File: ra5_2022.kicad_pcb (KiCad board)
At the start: 2 copper layers, 123 parts, among them CN1 KF250-3.5-2P-2, J1 USB_C_Receptacle, J2 MX15EDGRHC-3.5-2x03P, Q1 PJM2309PSC, SW1 SW_Push, SW2 SW_Push, U1 AP63203WU, U10 DB126V-5.0-2P-BK-P, U2 B0303S-1W_C883455, U3 ESP32-C6-MINI-1, U4 AMS1117-3.3, U5 ATM90E32AS-AU-R, U6 K3-2268P, U7 TLP291-4, U8 TLP291-4, U9 DB126V-5.0-2P-BK-P, Y1 ABM8G-16.384MHZ-18-D2Y-T

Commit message: Add MX15EDGRHC-3.5-2x03P footprint and update M90E32AS connector
Adds the new project-local footprint and repoints the M90E32AS
6-pin connector to it, plus resulting PCB layout and project
metadata updates.

Co-Authored-By: Claude Sonnet 5 <noreply@anthropic.com>
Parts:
- J2: footprint ra5_2022:CONN-TH_6P-P3.50x2.50_MAX_MX15EDGRHC-3.5-2x03P -> ra5_2022:MX15EDGRHC-3.5-2x03P
- moved J2 2.61 mm to (183.2, 100.0)
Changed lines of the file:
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@@
 		)
 	)
-	(footprint "ra5_2022:CONN-TH_6P-P3.50x2.50_MAX_MX15EDGRHC-3.5-2x03P"
+	(footprint "ra5_2022:MX15EDGRHC-3.5-2x03P"
 		(layer "F.Cu")
-		(at 184.775 102.075 90)
-		(descr "MAX (Cixi Maixu) MX15EDGRHC-3.5-2*03P-BK01-Cu-A, 6 position board-side header socket, right angle, THT, 3.5mm pitch (columns), 2.5mm row pitch, drill 1.4mm. Pad layout hand-derived from single-page mechanical datasheet (no explicit pinout diagram) - VERIFY against physical part/pin1 marking before fabrication. LCSC C49142489")
-		(tags "THT Terminal Block MAX MX15EDGRHC-3.5 2x03P pitch 3.5mm row 2.5mm drill 1.4mm C49142489")
+		(at 183.2 100 90)
 		(property "Reference" "J2"
-			(at 0 -4.8 90)
+			(at 0 -8.3 90)
+			(unlocked yes)
 			(layer "F.SilkS")
 			(effects
 				(font
 					(size 1 1)
-					(thickness 0.15)
+					(thickness 0.1)
 				)
 			)
 		)
 		(property "Value" "MX15EDGRHC-3.5-2x03P"
-			(at 0 4.8 90)
+			(at 0 -10.3 90)
+			(unlocked yes)
 			(layer "F.Fab")
 			(effects
@@
 		(property "Datasheet" "https://datasheet.lcsc.com/datasheet/pdf/3e53538744bd12542cc29a45b22c9fbc.pdf?productCode=C49142489"
 			(at 0 0 90)
+			(unlocked yes)
 			(layer "F.Fab")
 			(hide yes)
 			(effects
 				(font
-					(size 1.27 1.27)
+					(size 1 1)
+					(thickness 0.15)
 				)
 			)
@@
 		(property "Description" ""
 			(at 0 0 90)
+			(unlocked yes)
 			(layer "F.Fab")
 			(hide yes)
 			(effects
 				(font
-					(size 1.27 1.27)
+					(size 1 1)
+					(thickness 0.15)
 				)
 			)
 		)
-		(property "LCSC Part" "C49142489"
+		(property "Manufacturer" "Cixi Maixu Electronics (MAX)"
 			(at 0 0 90)
+			(unlocked yes)
 			(layer "F.Fab")
 			(hide yes)
 			(effects
 				(font
-					(size 1.27 1.27)
+					(size 1 1)
 					(thickness 0.15)
 				)
 			)
 		)
-		(property "Manufacturer" "Cixi Maixu Electronics (MAX)"
+		(property "MPN" "MX15EDGRHC-3.5-2*03P-BK01-Cu-A"
 			(at 0 0 90)
 			(unlocked yes)
@@
 			)
 		)
-		(property "MPN" "MX15EDGRHC-3.5-2*03P-BK01-Cu-A"
+		(property "LCSC Part" "C49142489"
+			(at 0 0 90)
+			(unlocked yes)
+			(layer "F.Fab")
+			(hide yes)
+			(effects
+				(font
+					(size 1 1)
+					(thickness 0.15)
+				)
+			)
+		)
+		(property "LCSC Part #" ""
 			(at 0 0 90)
 			(unlocked yes)
@@
 		(attr through_hole)
 		(duplicate_pad_numbers_are_jumpers no)
-		(fp_line
-			(start 5.65 -4)
-			(end 5.65 4)
-			(stroke
-				(width 0.15)
-				(type solid)
-			)
-			(layer "F.SilkS")
-		)
-		(fp_line
-			(start -5.65 -4)
-			(end 5.65 -4)
-			(stroke
-				(width 0.15)
-				(type solid)
-			)
-			(layer "F.SilkS")
-		)
-		(fp_line
-			(start 5.65 4)
-			(end -5.65 4)
-			(stroke
-				(width 0.15)
-				(type solid)
-			)
-			(layer "F.SilkS")
-		)
-		(fp_line
-			(start -5.65 4)
-			(end -5.65 -4)
+		(fp_rect
+			(start -5.65 -5.8)
+			(end 5.65 5.8)
 			(stroke
-				(width 0.15)
-				(type solid)
+				(width 0.1)
+				(type default)
 			)
+			(fill no)
 			(layer "F.SilkS")
 		)
-		(fp_line
-			(start 5.9 -4.25)
-			(end 5.9 4.25)
-			(stroke
-				(width 0.05)
-				(type solid)
-			)
-			(layer "F.CrtYd")
-		)
-		(fp_line
-			(start -5.9 -4.25)
-			(end 5.9 -4.25)
-			(stroke
-				(width 0.05)
-				(type solid)
-			)
-			(layer "F.CrtYd")
-		)
-		(fp_line
-			(start 5.9 4.25)
-			(end -5.9 4.25)
-			(stroke
-				(width 0.05)
-				(type solid)
-			)
-			(layer "F.CrtYd")
-		)
-		(fp_line
-			(start -5.9 4.25)
-			(end -5.9 -4.25)
-			(stroke
-				(width 0.05)
-				(type solid)
-			)
-			(layer "F.CrtYd")
-		)
 		(fp_text user "${REFERENCE}"
-			(at 0 0 90)
+			(at 0 -6.8 90)
+			(unlocked yes)
 			(layer "F.Fab")
 			(effects
@@
 			)
 		)
-		(pad "1" thru_hole rect
-			(at -3.5 -1.25 90)
-			(size 2.3 2.3)
+		(pad "1" thru_hole circle
+			(at -3.5 -4.7 90)
+			(size 2 2)
 			(drill 1.4)
 			(layers "*.Cu" "*.Mask")
@@
 			(pinfunction "1_1")
 			(pintype "unspecified")
+			(thermal_bridge_angle 90)
 		)
 		(pad "2" thru_hole circle
-			(at 0 -1.25 90)
-			(size 2.3 2.3)
+			(at -3.5 -2.2 90)
+			(size 2 2)
 			(drill 1.4)
 			(layers "*.Cu" "*.Mask")
@@
 			(pinfunction "2_2")
 			(pintype "unspecified")
+			(thermal_bridge_angle 90)
 		)
 		(pad "3" thru_hole circle
-			(at 3.5 -1.25 90)
-			(size 2.3 2.3)
+			(at 0 -4.7 90)
+			(size 2 2)
 			(drill 1.4)
 			(layers "*.Cu" "*.Mask")
@@
 			(pinfunction "3_3")
 			(pintype "unspecified")
+			(thermal_bridge_angle 90)
 		)
 		(pad "4" thru_hole circle
-			(at -3.5 1.25 90)
-			(size 2.3 2.3)
+			(at 0 -2.2 90)
+			(size 2 2)
 			(drill 1.4)
 			(layers "*.Cu" "*.Mask")
@@
 			(pinfunction "4_4")
 			(pintype "unspecified")
+			(thermal_bridge_angle 90)
 		)
 		(pad "5" thru_hole circle
-			(at 0 1.25 90)
-			(size 2.3 2.3)
+			(at 3.5 -4.7 90)
+			(size 2 2)
 			(drill 1.4)
 			(layers "*.Cu" "*.Mask")
@@
 			(pinfunction "5_5")
 			(pintype "unspecified")
+			(thermal_bridge_angle 90)
 		)
 		(pad "6" thru_hole circle
-			(at 3.5 1.25 90)
-			(size 2.3 2.3)
+			(at 3.5 -2.2 90)
+			(size 2 2)
 			(drill 1.4)
 			(layers "*.Cu" "*.Mask")
@@
 			(pinfunction "6_6")
 			(pintype "unspecified")
+			(thermal_bridge_angle 90)
 		)
 		(embedded_fonts no)
@@
 			(unit
 				(name "A")
-				(pins "SH" "B1" "B12" "A1" "A12" "B9" "A9" "B4" "A4" "A5" "B5" "A7" "B7"
+				(pins "SH" "A1" "A12" "B1" "B12" "A4" "A9" "B4" "B9" "A5" "B5" "A7" "B7"
 					"A6" "B6" "B10" "B11" "A3" "A2" "A10" "A11" "B3" "B2" "A8" "B8"
 				)
@@
 				(name "A")
 				(pins "8" "12" "13" "5" "6" "9" "10" "15" "16" "22" "23" "32" "33" "34"
-					"35" "3" "36" "37" "38" "39" "40" "41" "47" "42" "43" "44" "45" "46"
-					"2" "48" "49" "50" "51" "52" "53" "1" "11" "14" "4" "7" "21" "31" "30"
+					"35" "3" "2" "48" "1" "11" "49" "14" "50" "51" "52" "53" "47" "36" "37"
+					"38" "39" "40" "41" "42" "43" "44" "45" "46" "4" "7" "21" "31" "30"
 					"17" "18" "19" "20" "24" "25" "26" "27" "28" "29"
 				)

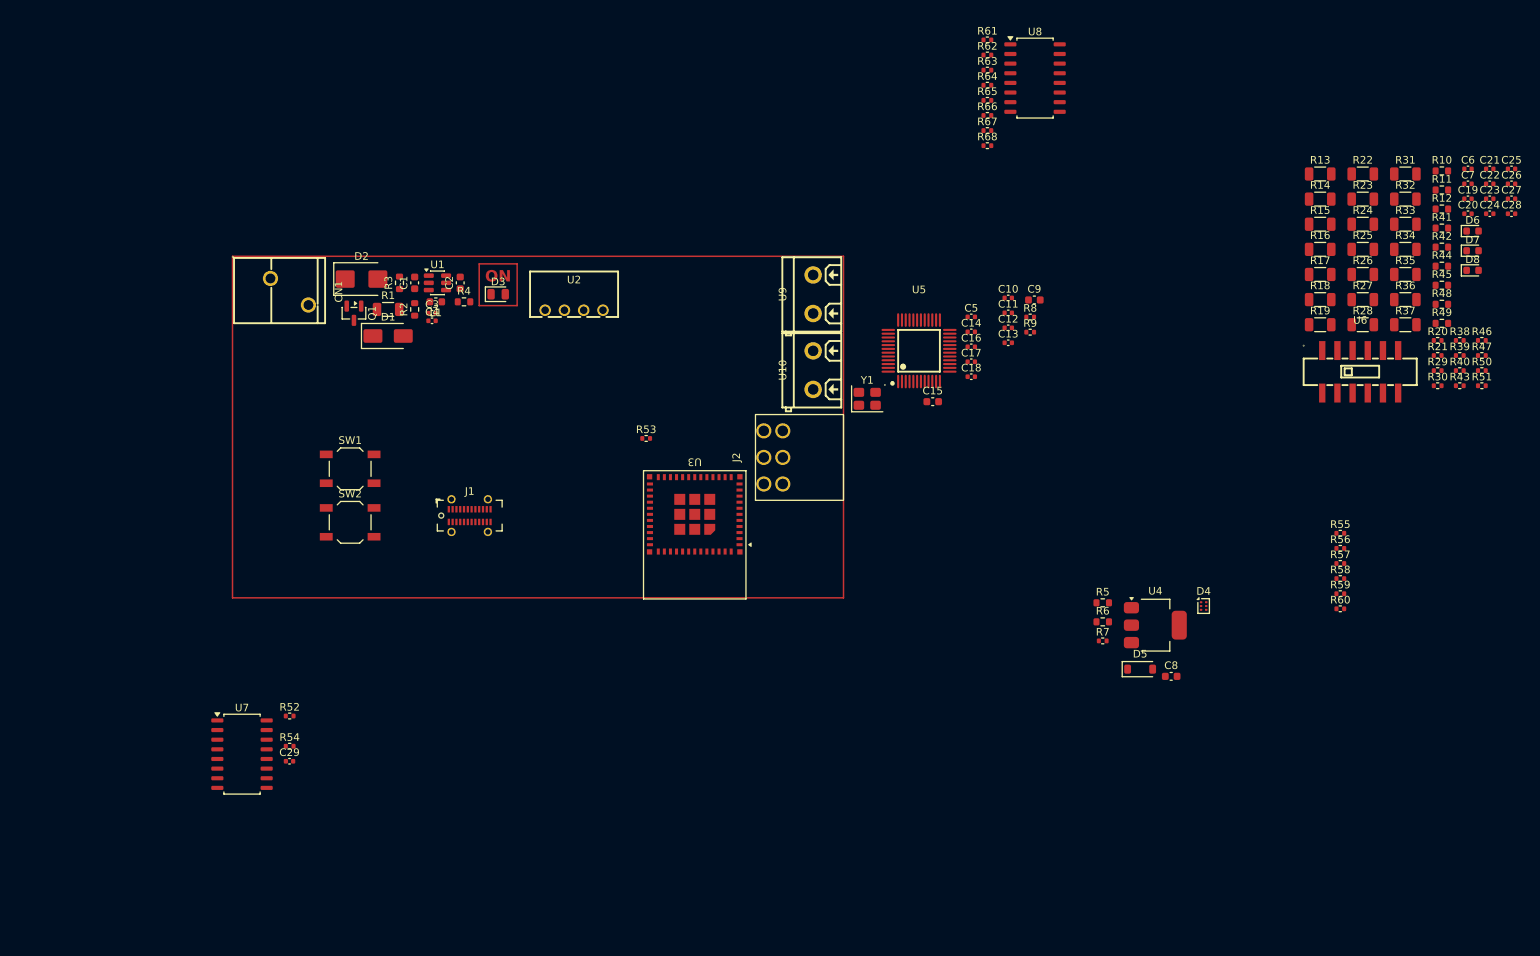
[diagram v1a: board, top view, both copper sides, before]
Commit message: Checkpoint: MCU/M90E32AS/power_source rework, PCB layout, new sheets, library imports
- Rework mcu.kicad_sch, m90e32as.kicad_sch and power_source.kicad_sch: PM0/PM1/
  IRQ0/IRQ1 isolation wiring for the M90E32AS, USB-C native USB wiring, and
  related connector updates.
- Add analog_io.kicad_sch and digital_io.kicad_sch hierarchical sheets.
- Update ra5_2022.kicad_pcb layout and ra5_2022.kicad_pro settings.
- Import several LCSC components into the project library (connectors,
  inductor, SOT/SOIC footprints, USB-C connectors, power module).
- Fix import_lcsc_component.sh to normalize the "LCSC Part" field name to
  "LCSC Part #" on imported footprints too (previously only on symbols).
- Ignore local .claude/ state (worktrees/session data) in .gitignore.

Co-Authored-By: Claude Sonnet 5 <noreply@anthropic.com>
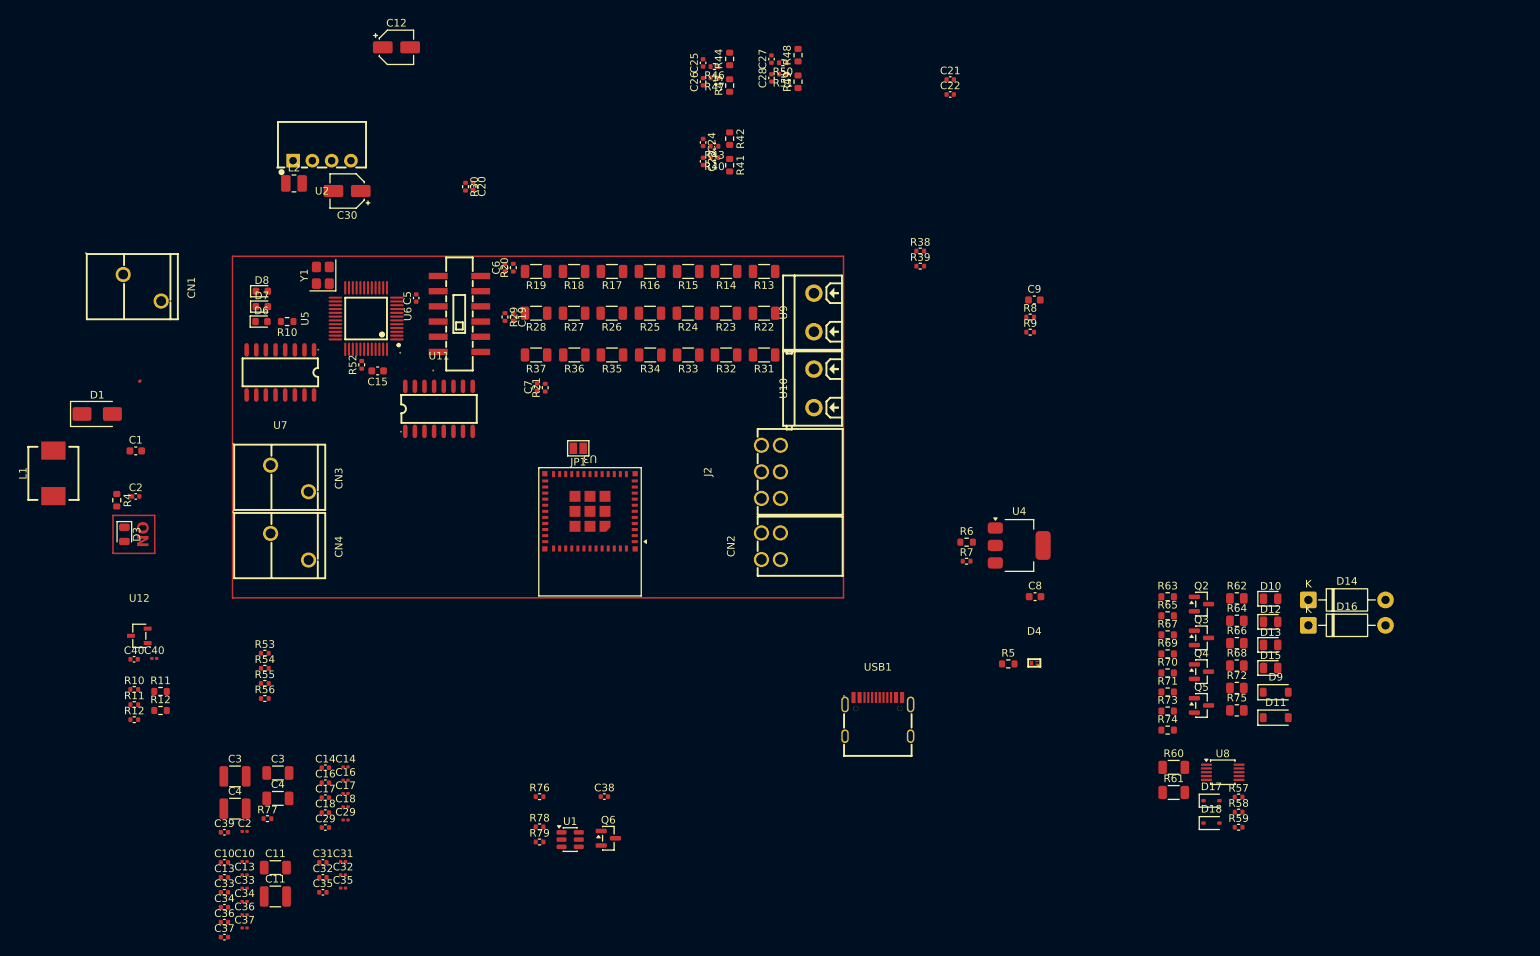
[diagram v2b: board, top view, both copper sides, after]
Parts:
- removed the C10 at (210.7, 79.0)
- removed the C11 at (210.7, 81.0)
- removed the C13 at (210.7, 84.9)
- removed the C14 at (205.8, 83.5)
- removed the C16 at (205.8, 85.4)
- removed the C17 at (205.8, 87.4)
- removed the C18 at (205.8, 89.4)
- removed the C29 at (116.0, 140.0)
- removed the C3 at (134.8, 81.0)
- removed the C4 at (134.8, 82.0)
- removed D2: SMBJ30A, Diode_SMD:D_SMB
- removed D5: D_Schottky, Diode_SMD:D_SOD-123
- removed J1: USB_C_Receptacle, Connector_USB:USB_C_Receptacle_GCT_USB4115-03-C
- removed Q1: PJM2309PSC, Package_TO_SOT_SMD:SOT-23
- removed R1: 10k, Resistor_SMD:R_1206_3216Metric
- removed the R11 at (267.8, 64.8)
- removed the R12 at (267.8, 67.3)
- removed R2: 22.1k, Resistor_SMD:R_0603_1608Metric
- removed R3: 5.36k, Resistor_SMD:R_0603_1608Metric
- removed SW1, SW2: SW_Push, Button_Switch_SMD:SW_SPST_TL3342
- added C10: 100nF, Capacitor_SMD:C_0201_0603Metric, F.Cu at (110.1, 153.2)
- added C10: 100nF, Capacitor_SMD:C_0402_1005Metric, F.Cu at (107.4, 153.4)
- added C11: 22uF, Capacitor_SMD:C_1206_3216Metric, F.Cu at (114.1, 154.0)
- added C11: 22uF, Capacitor_SMD:C_1210_3225Metric, F.Cu at (114.1, 157.8)
- added C13: 100nF, Capacitor_SMD:C_0402_1005Metric, F.Cu at (107.4, 155.3)
- added C13: 100nF, Capacitor_SMD:C_0201_0603Metric, F.Cu at (110.1, 155.0)
- added C14: 100nF, Capacitor_SMD:C_0201_0603Metric, F.Cu at (123.4, 140.8)
- added C14: 100nF, Capacitor_SMD:C_0402_1005Metric, F.Cu at (120.7, 140.9)
- added C16: 100nF, Capacitor_SMD:C_0402_1005Metric, F.Cu at (120.7, 142.9)
- added C16: 100nF, Capacitor_SMD:C_0201_0603Metric, F.Cu at (123.4, 142.5)
- added C17: 100nF, Capacitor_SMD:C_0201_0603Metric, F.Cu at (123.4, 144.3)
- added C17: 100nF, Capacitor_SMD:C_0402_1005Metric, F.Cu at (120.7, 144.8)
- added C18: 100nF, Capacitor_SMD:C_0402_1005Metric, F.Cu at (120.7, 146.8)
- added C18: 100nF, Capacitor_SMD:C_0201_0603Metric, F.Cu at (123.4, 146.0)
- added C2: 100nF, Capacitor_SMD:C_0201_0603Metric, F.Cu at (110.1, 149.3)
- added C29: 100nF, Capacitor_SMD:C_0402_1005Metric, F.Cu at (120.7, 148.8)
- added C29: 100nF, Capacitor_SMD:C_0201_0603Metric, F.Cu at (123.4, 147.8)
- added C3: 22uF, Capacitor_SMD:C_1210_3225Metric, F.Cu at (108.8, 142.0)
- added C3: 22uF, Capacitor_SMD:C_1206_3216Metric, F.Cu at (114.5, 141.6)
- added C30: 10uF, Capacitor_SMD:CP_Elec_4x5.4, F.Cu at (123.6, 64.9)
- added C31: 100nF, Capacitor_SMD:C_0402_1005Metric, F.Cu at (120.4, 153.4)
- added C31: 100nF, Capacitor_SMD:C_0201_0603Metric, F.Cu at (123.1, 153.2)
- added C32: 100nF, Capacitor_SMD:C_0201_0603Metric, F.Cu at (123.1, 155.0)
- added C32: 100nF, Capacitor_SMD:C_0402_1005Metric, F.Cu at (120.4, 155.3)
- added C33: 100nF, Capacitor_SMD:C_0201_0603Metric, F.Cu at (110.1, 156.7)
- added C33: 100nF, Capacitor_SMD:C_0402_1005Metric, F.Cu at (107.4, 157.3)
- added C34: 100nF, Capacitor_SMD:C_0402_1005Metric, F.Cu at (107.4, 159.3)
- added C34: 100nF, Capacitor_SMD:C_0201_0603Metric, F.Cu at (110.1, 158.5)
- added C35: 100nF, Capacitor_SMD:C_0402_1005Metric, F.Cu at (120.4, 157.3)
- added C35: 100nF, Capacitor_SMD:C_0201_0603Metric, F.Cu at (123.1, 156.7)
- added C36: 100nF, Capacitor_SMD:C_0402_1005Metric, F.Cu at (107.4, 161.2)
- added C36: 100nF, Capacitor_SMD:C_0201_0603Metric, F.Cu at (110.1, 160.2)
- added C37: 100nF, Capacitor_SMD:C_0402_1005Metric, F.Cu at (107.4, 163.2)
- added C37: 100nF, Capacitor_SMD:C_0201_0603Metric, F.Cu at (110.1, 162.0)
- added C38: 56pF, Capacitor_SMD:C_0402_1005Metric, F.Cu at (157.5, 144.7)
- added C39: 100nF, Capacitor_SMD:C_0402_1005Metric, F.Cu at (107.4, 149.4)
- added C4: 22uF, Capacitor_SMD:C_1210_3225Metric, F.Cu at (108.8, 146.3)
- added C4: 22uF, Capacitor_SMD:C_1206_3216Metric, F.Cu at (114.5, 144.9)
- added C40: 100nF, Capacitor_SMD:C_0201_0603Metric, F.Cu at (98.2, 126.5)
- added C40: 100nF, Capacitor_SMD:C_0402_1005Metric, F.Cu at (95.5, 126.6)
- added CN2: MX15EDGRHC-3.5-2*02P-BK01-CU-A, ra5_2022:CONN-TH_4P-P3.50_JL15EDGRHC-35002B01, F.Cu at (179.4, 111.7)
- added CN3: KF250-3.5-2P-2, ra5_2022:CONN-TH_P3.50_KF250-3.5-2P-2, F.Cu at (116.0, 102.8)
- added CN4: KF250-3.5-2P-2, ra5_2022:CONN-TH_P3.50_KF250-3.5-2P-2, F.Cu at (116.0, 111.8)
- added D10: LED, LED_SMD:LED_0805_2012Metric, F.Cu at (245.3, 118.6)
- added D11: BZT52C3V3, Diode_SMD:D_SOD-123, F.Cu at (245.9, 134.3)
- added D12: LED, LED_SMD:LED_0805_2012Metric, F.Cu at (245.3, 121.7)
- added D13: LED, LED_SMD:LED_0805_2012Metric, F.Cu at (245.3, 124.7)
- added D14: 1N4004W, Diode_THT:D_DO-41_SOD81_P10.16mm_Horizontal, F.Cu at (250.2, 118.8)
- added D15: LED, LED_SMD:LED_0805_2012Metric, F.Cu at (245.3, 127.7)
- added D16: 1N4004W, Diode_THT:D_DO-41_SOD81_P10.16mm_Horizontal, F.Cu at (250.2, 122.1)
- added D17: SD103AWS, Diode_SMD:D_SOD-323, F.Cu at (237.5, 145.2)
- added D18: SD103AWS, Diode_SMD:D_SOD-323, F.Cu at (237.5, 148.2)
- added D9: BZT52C3V3, Diode_SMD:D_SOD-123, F.Cu at (245.9, 130.9)
- added JP1: SolderJumper_2_Open, Jumper:SolderJumper-2_P1.3mm_Open_Pad1.0x1.5mm, F.Cu at (154.1, 98.8)
- added L2: 6.8uH, Inductor_SMD:L_1008_2520Metric, F.Cu at (116.6, 63.9)
- added Q2: BC817, Package_TO_SOT_SMD:SOT-23, F.Cu at (236.2, 119.3)
- added Q3: BC817, Package_TO_SOT_SMD:SOT-23, F.Cu at (236.2, 123.8)
- added Q4: BC817, Package_TO_SOT_SMD:SOT-23, F.Cu at (236.2, 128.2)
- added Q5: BC817, Package_TO_SOT_SMD:SOT-23, F.Cu at (236.2, 132.7)
- added Q6: BC817, Package_TO_SOT_SMD:SOT-23, F.Cu at (158.0, 150.2)
- added R10: 270R, Resistor_SMD:R_0402_1005Metric, F.Cu at (95.6, 130.6)
- added R11: 270R, Resistor_SMD:R_0402_1005Metric, F.Cu at (95.6, 132.6)
- added R11: 80R, Resistor_SMD:R_0603_1608Metric, F.Cu at (99.0, 130.8)
- added R12: 80R, Resistor_SMD:R_0603_1608Metric, F.Cu at (99.0, 133.3)
- added R12: 270R, Resistor_SMD:R_0402_1005Metric, F.Cu at (95.6, 134.6)
- added R69: 270R, Resistor_SMD:R_0603_1608Metric, F.Cu at (231.7, 125.9)
- added R70: 270R, Resistor_SMD:R_0603_1608Metric, F.Cu at (231.7, 128.4)
- added R71: 1K, Resistor_SMD:R_0603_1608Metric, F.Cu at (231.7, 130.9)
- added R72: 10k, Resistor_SMD:R_0805_2012Metric, F.Cu at (240.8, 130.4)
- added R73: 270R, Resistor_SMD:R_0603_1608Metric, F.Cu at (231.7, 133.4)
- added R74: 1K, Resistor_SMD:R_0603_1608Metric, F.Cu at (231.7, 135.9)
- added R75: 10k, Resistor_SMD:R_0805_2012Metric, F.Cu at (240.8, 133.3)
- added R76: 100k, Resistor_SMD:R_0402_1005Metric, F.Cu at (149.0, 144.7)
- added R77: 22.1k, Resistor_SMD:R_0402_1005Metric, F.Cu at (113.1, 147.6)
- added R78: 100k, Resistor_SMD:R_0402_1005Metric, F.Cu at (149.0, 148.7)
- added R79: 100k, Resistor_SMD:R_0402_1005Metric, F.Cu at (149.0, 150.7)
- added U11: ISO7741N1-Y, ra5_2022:SOIC-16_L9.9-W3.9-P1.27-LS6.0-BL-1, F.Cu at (135.7, 93.6)
- added U12: JTD6206-3.3V, ra5_2022:SOT-23-3_L3.0-W1.7-P0.95-LS2.9-BR, F.Cu at (96.2, 123.5)
- added USB1: HYCW498-USBC16-735B, ra5_2022:USB-C-SMD_HYCW498-USBC16-735B, F.Cu at (193.5, 134.2)
- C12: value 100nF -> 10uF; footprint Capacitor_SMD:C_0402_1005Metric -> Capacitor_SMD:CP_Elec_4x5.4
- C2: footprint Capacitor_SMD:C_0603_1608Metric -> Capacitor_SMD:C_0402_1005Metric
- D1: value 1SMA4744A -> SS16
- D3: value YLED0805R -> LED
- D4: value PESD5V0L4UF -> PESD5V0L2UM,315; footprint Package_TO_SOT_SMD:SOT-886 -> ra5_2022:SOT-883-3_L1.0-W0.6-BR
- L1: value 39uH -> 10uH; footprint Inductor_SMD:L_0603_1608Metric -> ra5_2022:IND-SMD_L7.0-W6.6
- R53, R55: value 430R -> 4.7k
- R54, R56: value 560R -> 4.7k
- R57: value 270R -> 10k
- R58: value 560R -> 10k
- R59: value 430R -> 10k
- R60: value 560R -> 100R; footprint Resistor_SMD:R_0402_1005Metric -> Resistor_SMD:R_1206_3216Metric
- R61: value 430R -> 100R; footprint Resistor_SMD:R_0402_1005Metric -> Resistor_SMD:R_1206_3216Metric
- R62, R64, R66, R68: value 560R -> 10k; footprint Resistor_SMD:R_0402_1005Metric -> Resistor_SMD:R_0805_2012Metric
- R63, R67: value 430R -> 39k; footprint Resistor_SMD:R_0402_1005Metric -> Resistor_SMD:R_0603_1608Metric
- R65: value 430R -> 270R; footprint Resistor_SMD:R_0402_1005Metric -> Resistor_SMD:R_0603_1608Metric
- U1: value AP63203WU -> TPS54202DDC; footprint Package_TO_SOT_SMD:TSOT-23-6 -> Package_TO_SOT_SMD:SOT-23-6
- U2: value B0303S-1W_C883455 -> B0303S-1WR2; footprint ra5_2022:PWRM-TH_B2415S-1W -> ra5_2022:PWRM-TH_BXXXXS-1WR2
- U7: value TLP291-4 -> ISO7742N1-Y; footprint Package_SO:SOIC-16_4.55x10.3mm_P1.27mm -> ra5_2022:SOIC-16_L9.9-W3.9-P1.27-LS6.0-BL-1
- U8: value TLP291-4 -> ADS1115IDGS; footprint Package_SO:SOIC-16_4.55x10.3mm_P1.27mm -> Package_SO:TSSOP-10_3x3mm_P0.5mm
- moved D6 160.0 mm to (112.3, 82.1)
- moved D7 159.7 mm to (112.4, 80.1)
- moved D8 159.5 mm to (112.4, 78.1)
- moved R10 153.4 mm to (115.7, 82.1), turned to 180 degrees
- moved R55 143.1 mm to (112.8, 129.8)
- moved R56 143.1 mm to (112.8, 131.8)
- moved C20 131.1 mm to (140.2, 64.3), turned to -90 degrees
- moved R30 130.7 mm to (139.2, 64.3), turned to -90 degrees
- moved C6 127.5 mm to (144.4, 75.0), turned to 90 degrees
- moved C19 126.7 mm to (145.5, 81.5), turned to -90 degrees
- moved C7 125.5 mm to (148.6, 90.7), turned to 90 degrees
- moved R29 123.1 mm to (144.4, 81.5), turned to -90 degrees
- moved R20 122.2 mm to (145.5, 75.0), turned to 90 degrees
- moved U6 118.9 mm to (138.4, 81.1), turned to 90 degrees
- moved R21 117.7 mm to (149.7, 90.8), turned to 90 degrees
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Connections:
- net /MCU/+5V_USB renamed +5V_USB
- C12 pad 1: /MCU/EN -> VDD
- C2 pad 1: Net-(U1-SW) -> Net-(U1-BOOT)
- C2 pad 2: /Power Source/BST -> Net-(U1-SW)
- C9 pad 2: /MCU/+3V3_USB -> VDD
- D1 pad 2: GND -> VCC
- D4 pad 1: /MCU/USB_DP -> /MCU/USB_DN
- D4 pad 2: GND -> /MCU/USB_DP
- D4 pad 3: /MCU/USB_DN -> GND
- D6 pad 1: Net-(D6-K) -> GND2
- D6 pad 2: /MCU/M90E32AS/ZX0 -> Net-(D6-A)
- D7 pad 1: Net-(D7-K) -> GND2
- D7 pad 2: /MCU/M90E32AS/ZX1 -> Net-(D7-A)
- D8 pad 1: Net-(D8-K) -> GND2
- D8 pad 2: /MCU/M90E32AS/ZX2 -> Net-(D8-A)
- J2 pad 1: /MCU/M90E32AS/IR+ -> /MCU/M90E32AS/IT+
- J2 pad 2: /MCU/M90E32AS/IR- -> /MCU/M90E32AS/IT-
- J2 pad 5: /MCU/M90E32AS/IT+ -> /MCU/M90E32AS/IR+
- J2 pad 6: /MCU/M90E32AS/IT- -> /MCU/M90E32AS/IR-
- R10 pad 1: Net-(D6-K) -> /MCU/M90E32AS/ZX0
- R10 pad 2: GND2 -> Net-(D6-A)
- R53 pad 1: /MCU/M90E32AS/IO18 -> VDD
- R54 pad 1: VDD2 -> Net-(U7-EN2)
- R54 pad 2: /MCU/M90E32AS/SCLK -> VDD2
- R55 pad 1: /MCU/IO19 -> VDD
- R55 pad 2: Net-(R55-Pad2) -> Net-(U11-EN1)
- R56 pad 1: VDD2 -> Net-(U11-EN2)
- R56 pad 2: /MCU/M90E32AS/SDI -> VDD2
- R57 pad 1: /MCU/M90E32AS/SDO -> /MCU/IO15
- R57 pad 2: Net-(R57-Pad2) -> VDD
- R58 pad 1: VDD -> /MCU/IO3
- R58 pad 2: /MCU/IO20 -> VDD
- R59 pad 1: /MCU/IO21 -> /MCU/IO2
- R59 pad 2: Net-(R59-Pad2) -> VDD
- R60 pad 1: VDD2 -> /MCU/Analog IO/AIN0
- R60 pad 2: /MCU/M90E32AS/CS -> /MCU/Analog IO/AIN1
- R61 pad 1: /MCU/M90E32AS/IRQ0 -> /MCU/Analog IO/AIN2
- R61 pad 2: Net-(R61-Pad2) -> /MCU/Analog IO/AIN2-
- R62 pad 1: VDD -> /MCU/Digital IO/DI1
- R62 pad 2: /MCU/IO22 -> /MCU/Digital IO/DIN1_MCU
- R63 pad 1: /MCU/M90E32AS/IRQ1 -> GND
- R63 pad 2: Net-(R63-Pad2) -> Net-(D9-A)
- R64 pad 1: VDD -> Net-(Q2-B)
- R64 pad 2: /MCU/IO23 -> /MCU/Digital IO/DIN1_MCU
- R65 pad 1: /MCU/IO0 -> Net-(D10-A)
- R65 pad 2: Net-(R65-Pad2) -> VDD
- R66 pad 1: VDD2 -> /MCU/Digital IO/DI2
- R66 pad 2: /MCU/M90E32AS/PM0 -> /MCU/Digital IO/DIN2_MCU
- R67 pad 1: /MCU/IO1 -> GND
- R67 pad 2: Net-(R67-Pad2) -> Net-(D11-A)
- R68 pad 1: VDD2 -> Net-(Q3-B)
- R68 pad 2: /MCU/M90E32AS/PM1 -> /MCU/Digital IO/DIN2_MCU
- U1 pad 1: VDD -> GND
- U1 pad 2: /Power Source/EN -> Net-(U1-SW)
- U1 pad 4: GND -> /Power Source/FB
- U1 pad 5: Net-(U1-SW) -> /Power Source/EN
- U1 pad 6: /Power Source/BST -> Net-(U1-BOOT)
- U10 pad 1: /MCU/M90E32AS/T -> GND2
- U10 pad 2: GND2 -> /MCU/M90E32AS/T
- U2 pad 2: VDD -> Net-(U2-+Vin)
- U2 pad 4: VDD2 -> Net-(U12-VIN)
- U3 pad 24: /MCU/M90E32AS/IO18 -> /MCU/IO18
- U4 pad 2: /MCU/+3V3_USB -> VDD
- U5 pad 30: /MCU/M90E32AS/IRQ0 -> /MCU/IRQ1
- U5 pad 31: /MCU/M90E32AS/IRQ1 -> /MCU/IRQ0
- U5 pad 33: /MCU/M90E32AS/PM0 -> /MCU/PM1
- U5 pad 34: /MCU/M90E32AS/PM1 -> /MCU/PM0
- U5 pad 39: /MCU/M90E32AS/SDO -> /MCU/M90E32AS/MISO
- U5 pad 40: /MCU/M90E32AS/SDI -> /MCU/M90E32AS/MOSI
- U5 pad 44: unconnected-(U5-DGND-Pad44) -> GND2
- U6 pad 1: /MCU/M90E32AS/V2P_SW -> /MCU/M90E32AS/I2N_SW
- U6 pad 10: /MCU/M90E32AS/I2N_SW -> /MCU/M90E32AS/V2P_SW
- U6 pad 11: /MCU/M90E32AS/I2N -> /MCU/M90E32AS/V2P
- U6 pad 2: /MCU/M90E32AS/V2P -> /MCU/M90E32AS/I2N
- U7 pad 1: Net-(R59-Pad2) -> VDD
- U7 pad 10: /MCU/M90E32AS/SCLK -> Net-(U7-EN2)
- U7 pad 11: GND -> /MCU/IRQ1
- U7 pad 12: /MCU/IO20 -> /MCU/IRQ0
- U7 pad 13: GND2 -> /MCU/PM1
- U7 pad 14: /MCU/M90E32AS/SDI -> /MCU/PM0
- U7 pad 16: /MCU/M90E32AS/CS -> VDD2
- U7 pad 3: Net-(R55-Pad2) -> /MCU/IO0
- U7 pad 4: GND -> /MCU/IO1
- U7 pad 5: Net-(R57-Pad2) -> /MCU/IO22
- U7 pad 6: GND2 -> /MCU/IO23
- U8 pad 1: Net-(R61-Pad2) -> GND
- U8 pad 10: /MCU/M90E32AS/PM1 -> /MCU/IO2
- U8 pad 2: GND2 -> /MCU/IO15
- U8 pad 3: Net-(R63-Pad2) -> GND
- U8 pad 4: GND2 -> /MCU/Analog IO/AIN0
- U8 pad 5: Net-(R65-Pad2) -> /MCU/Analog IO/AIN1
- U8 pad 6: GND -> /MCU/Analog IO/AIN2
- U8 pad 7: Net-(R67-Pad2) -> /MCU/Analog IO/AIN2-
- U8 pad 8: GND -> VDD
- U8 pad 9: GND2 -> /MCU/IO3
- U9 pad 1: /MCU/M90E32AS/R -> /MCU/M90E32AS/S
- U9 pad 2: /MCU/M90E32AS/S -> /MCU/M90E32AS/R

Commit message: Swap U7 isolator from ISO7742N1-Y to CS817X20LS
Only PM0/PM1 need to cross the M90E32AS isolation barrier now (IRQ0/IRQ1
dropped in favor of freeing GPIOs for the 4G modem RTS/CTS), so the
4-channel 2fwd/2rev isolator is replaced with the 2-channel, same-direction,
default-LOW CS817X20LS. Updates schematic, PCB footprint/routing and BOM.

Co-Authored-By: Claude Sonnet 5 <noreply@anthropic.com>
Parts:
- removed the C40 at (98.2, 126.5)
- removed the C40 at (95.5, 126.6)
- removed R53, R54: 4.7k, Resistor_SMD:R_0402_1005Metric
- added C40: 10uF, Capacitor_SMD:C_0603_1608Metric, F.Cu at (190.9, 147.5)
- U7: value ISO7742N1-Y -> CS817X20LS; footprint ra5_2022:SOIC-16_L9.9-W3.9-P1.27-LS6.0-BL-1 -> ra5_2022:SOIC-8_L4.9-W3.9-P1.27-LS6.0-BL
- moved U7 92.4 mm to (183.8, 150.2), turned to 0 degrees
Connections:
- U3 pad 19: /MCU/IO14 -> unconnected-(U3-IO14-Pad19)
- U3 pad 28: /MCU/IO22 -> unconnected-(U3-IO22-Pad28)
- U3 pad 29: /MCU/IO23 -> unconnected-(U3-IO23-Pad29)
- U5 pad 30: /MCU/IRQ1 -> unconnected-(U5-IRQ0-Pad30)
- U5 pad 31: /MCU/IRQ0 -> unconnected-(U5-IRQ1-Pad31)
- U7 pad 2: GND -> /MCU/IO0
- U7 pad 3: /MCU/IO0 -> /MCU/IO1
- U7 pad 4: /MCU/IO1 -> GND
- U7 pad 5: /MCU/IO22 -> GND2
- U7 pad 6: /MCU/IO23 -> /MCU/PM1
- U7 pad 7: Net-(U7-EN1) -> /MCU/PM0
- U7 pad 8: GND -> VDD2
